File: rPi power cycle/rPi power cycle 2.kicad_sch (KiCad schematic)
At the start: 9 parts, among them J2 BATT, Q1 BC548

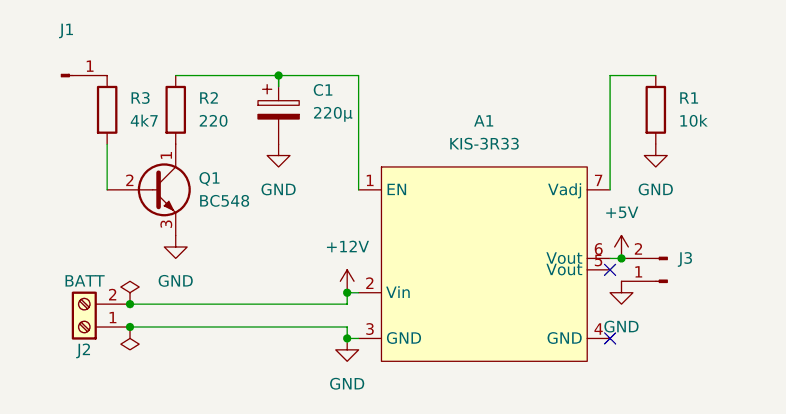
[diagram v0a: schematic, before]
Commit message: Use via to simulate internal connections
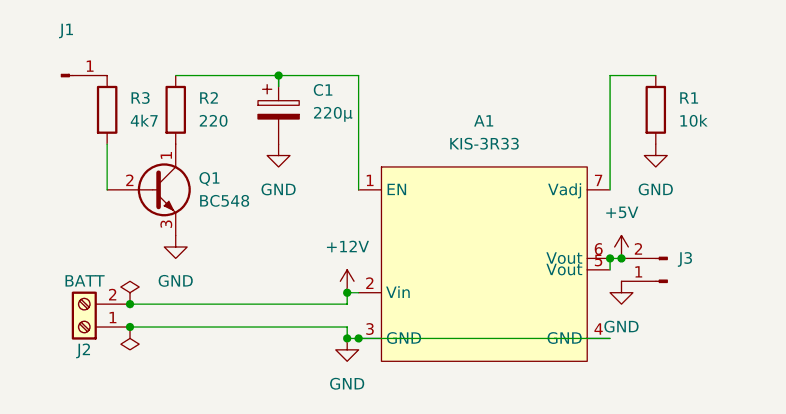
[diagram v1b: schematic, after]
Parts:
- J1: footprint Connector_PinHeader_1.00mm:PinHeader_1x01_P1.00mm_Vertical -> (none)
- J3: footprint TerminalBlock:TerminalBlock_bornier-2_P5.08mm -> (none)
- Q1: footprint Package_TO_SOT_THT:TO-92_HandSolder -> (none)
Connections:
- net +5V: now also A1.5 (Vout)
- net GND: now also A1.4 (GND)
- no-connect marks 2 -> 0
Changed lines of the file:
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@@
   (junction (at 121.92 83.82) (diameter 0) (color 0 0 0 0)
   )
+  (junction (at 123.19 88.9) (diameter 0) (color 0 0 0 0)
+  )
+  (junction (at 151.13 80.01) (diameter 0) (color 0 0 0 0)
+  )
   (junction (at 121.92 88.9) (diameter 0) (color 0 0 0 0)
   )
@@
   (junction (at 152.4 80.01) (diameter 0) (color 0 0 0 0)
   )
-  (no_connect (at 151.13 81.28))
-  (no_connect (at 151.13 88.9))
   (wire (pts (xy 97.79 87.63) (xy 121.92 87.63))
     (stroke (width 0) (type default) (color 0 0 0 0))
@@
     (stroke (width 0) (type default) (color 0 0 0 0))
   )
+  (wire (pts (xy 123.19 88.9) (xy 151.13 88.9))
+    (stroke (width 0) (type default) (color 0 0 0 0))
+  )
   (wire (pts (xy 121.92 83.82) (xy 123.19 83.82))
+    (stroke (width 0) (type default) (color 0 0 0 0))
+  )
+  (wire (pts (xy 151.13 80.01) (xy 151.13 81.28))
     (stroke (width 0) (type default) (color 0 0 0 0))
   )
@@
       (effects (font (size 1.27 1.27)) (justify left))
     )
-    (property "Footprint" "Package_TO_SOT_THT:TO-92_HandSolder" (id 2) (at 105.41 74.295 0)
+    (property "Footprint" "" (id 2) (at 105.41 74.295 0)
       (effects (font (size 1.27 1.27) italic) (justify left) hide)
     )
@@
       (effects (font (size 1.27 1.27)) (justify right))
     )
-    (property "Footprint" "TerminalBlock:TerminalBlock_bornier-2_P5.08mm" (id 2) (at 157.48 82.55 0)
+    (property "Footprint" "" (id 2) (at 157.48 82.55 0)
       (effects (font (size 1.27 1.27)) hide)
     )
@@
     (property "Reference" "J1" (id 0) (at 90.805 54.61 0))
     (property "Value" "" (id 1) (at 90.805 57.15 0))
-    (property "Footprint" "Connector_PinHeader_1.00mm:PinHeader_1x01_P1.00mm_Vertical" (id 2) (at 90.17 59.69 0)
+    (property "Footprint" "" (id 2) (at 90.17 59.69 0)
       (effects (font (size 1.27 1.27)) hide)
     )
@@
     )
     (path "/9eba85d4-45b3-433f-bb51-89323b97cd8e"
-      (reference "J1") (unit 1) (value "RPi GPIO") (footprint "Connector_PinHeader_1.00mm:PinHeader_1x01_P1.00mm_Vertical")
+      (reference "J1") (unit 1) (value "RPi GPIO") (footprint "Connector_PinHeader_2.54mm:PinHeader_1x01_P2.54mm_Vertical")
     )
     (path "/82256131-df4b-459a-bd03-b206fea6aa4c"
@@
     )
     (path "/4150e76b-c688-40fd-af7a-ebd5c492c337"
-      (reference "J3") (unit 1) (value "RPi PWR") (footprint "TerminalBlock:TerminalBlock_bornier-2_P5.08mm")
+      (reference "J3") (unit 1) (value "RPi PWR") (footprint "Connector_PinHeader_2.54mm:PinHeader_1x02_P2.54mm_Vertical")
     )
     (path "/010d499c-6db7-48dc-ab87-796ca70e4bcf"
-      (reference "Q1") (unit 1) (value "BC548") (footprint "Package_TO_SOT_THT:TO-92_HandSolder")
+      (reference "Q1") (unit 1) (value "BC548") (footprint "Package_TO_SOT_THT:TO-92_Wide")
     )
     (path "/dd3da890-32ef-4a5a-aea4-e5d2141f1ff1"

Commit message: Add Power netclass and update track widths
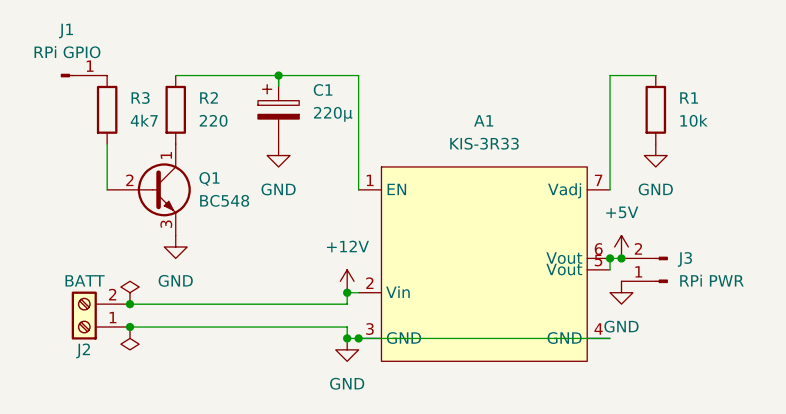
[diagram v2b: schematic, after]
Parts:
- J1: value (none) -> RPi GPIO; footprint (none) -> Connector_PinHeader_2.54mm:PinHeader_1x01_P2.54mm_Vertical
- J3: value (none) -> RPi PWR; footprint (none) -> Connector_PinHeader_2.54mm:PinHeader_1x02_P2.54mm_Vertical
- Q1: footprint (none) -> Package_TO_SOT_THT:TO-92_Wide
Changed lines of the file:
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@@
       (effects (font (size 1.27 1.27)) (justify left))
     )
-    (property "Footprint" "" (id 2) (at 105.41 74.295 0)
+    (property "Footprint" "Package_TO_SOT_THT:TO-92_Wide" (id 2) (at 105.41 74.295 0)
       (effects (font (size 1.27 1.27) italic) (justify left) hide)
     )
@@
       (effects (font (size 1.27 1.27)) (justify right))
     )
-    (property "Value" "" (id 1) (at 158.75 82.5499 0)
+    (property "Value" "RPi PWR" (id 1) (at 158.75 82.5499 0)
       (effects (font (size 1.27 1.27)) (justify right))
     )
-    (property "Footprint" "" (id 2) (at 157.48 82.55 0)
+    (property "Footprint" "Connector_PinHeader_2.54mm:PinHeader_1x02_P2.54mm_Vertical" (id 2) (at 157.48 82.55 0)
       (effects (font (size 1.27 1.27)) hide)
     )
@@
     (in_bom yes) (on_board yes) (fields_autoplaced)
     (property "Reference" "J1" (id 0) (at 90.805 54.61 0))
-    (property "Value" "" (id 1) (at 90.805 57.15 0))
-    (property "Footprint" "" (id 2) (at 90.17 59.69 0)
+    (property "Value" "RPi GPIO" (id 1) (at 90.805 57.15 0))
+    (property "Footprint" "Connector_PinHeader_2.54mm:PinHeader_1x01_P2.54mm_Vertical" (id 2) (at 90.17 59.69 0)
       (effects (font (size 1.27 1.27)) hide)
     )
